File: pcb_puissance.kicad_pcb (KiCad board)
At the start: 2 copper layers, 126.5 x 120.5 mm, 40 parts, among them J1 1755736, J10 Conn_01x02, J11 Conn_01x02, J2 1755736, J3 1755736, J4 1755736, J5 1755736, J6 1755736, J7 1755736, J8 1755736, J9 Conn_01x02, K1 SRD-05VDC-SL-C

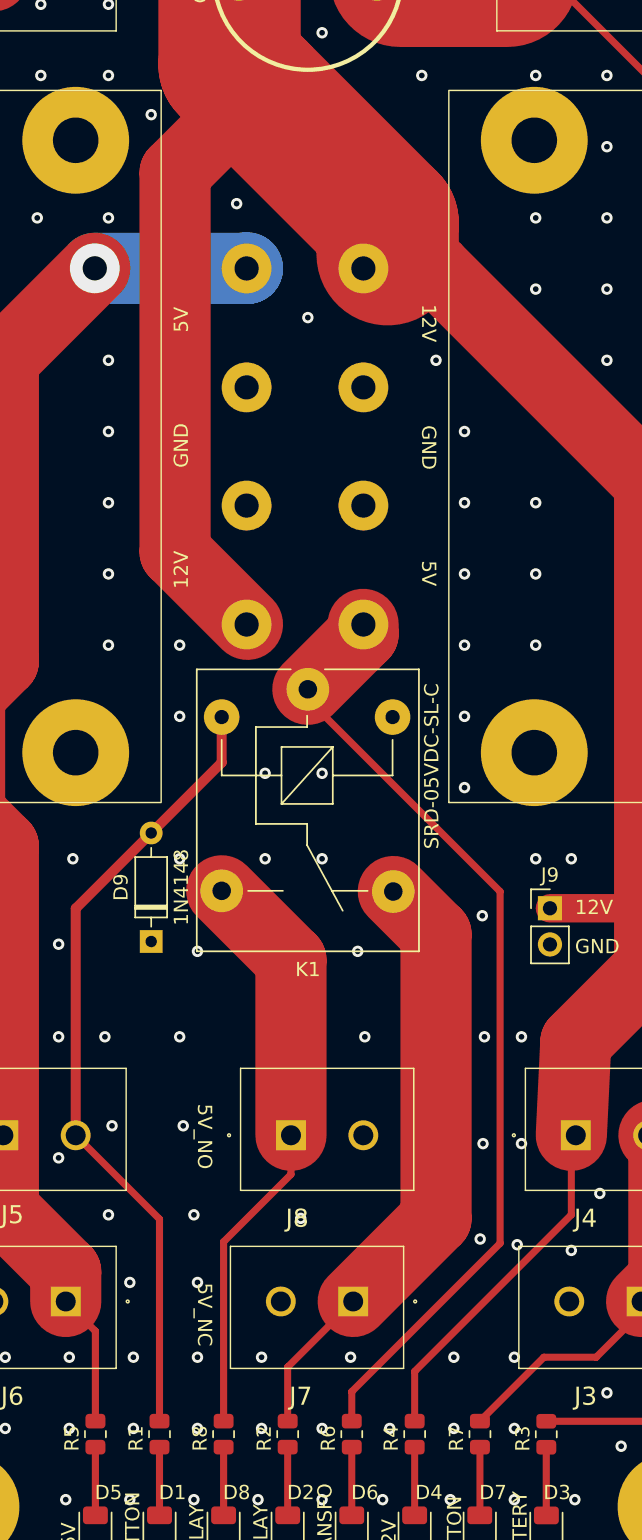
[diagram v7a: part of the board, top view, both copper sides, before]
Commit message: Ajout noms transfos +visibles
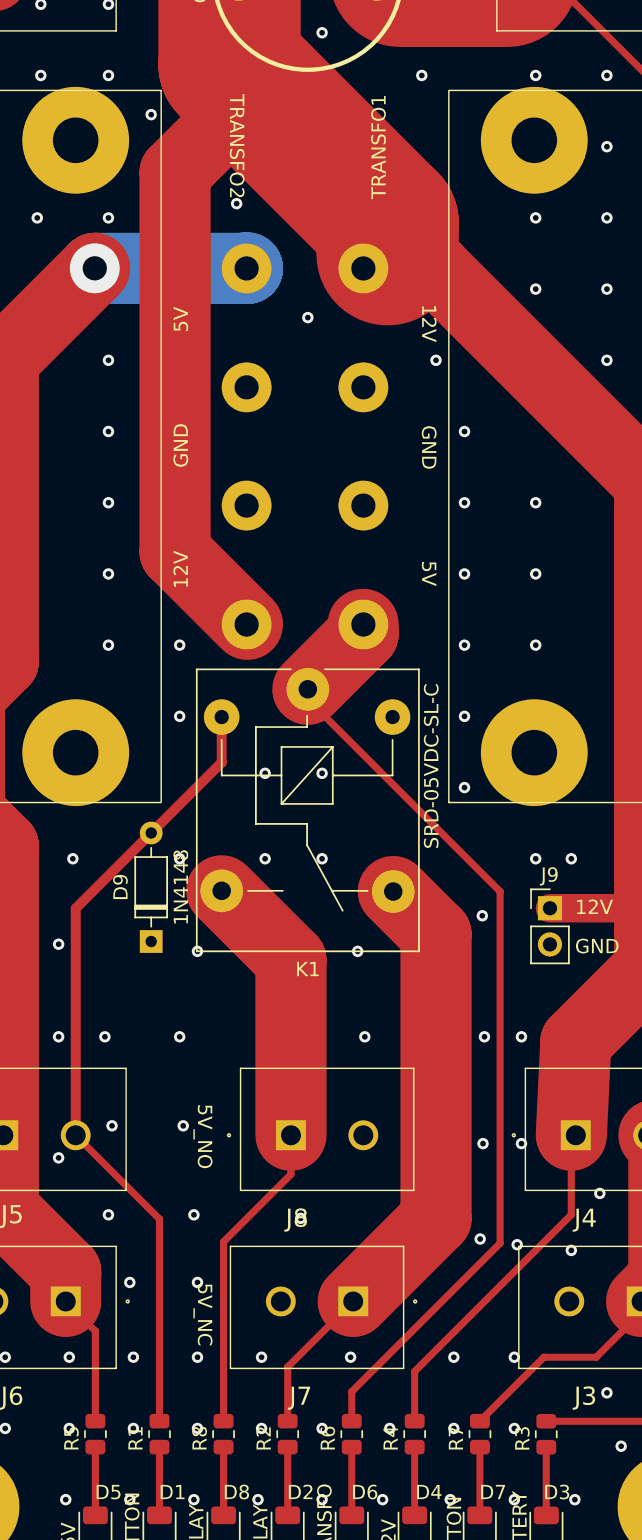
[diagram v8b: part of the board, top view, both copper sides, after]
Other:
- board text added: "TRANSFO1"
- board text added: "TRANSFO2"
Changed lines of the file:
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@@
     (fp_line (start 1 0.625) (end -1 0.625)
       (stroke (width 0.1) (type solid)) (layer "F.Fab"))
-    (pad "1" smd roundrect (at -0.9125 0 90) (size 1.025 1.4) (layers "F.Cu" "F.Paste" "F.Mask") (roundrect_rratio 0.243902)
+    (pad "1" smd roundrect (at -0.9125 0 90) (size 1.025 1.4) (layers "F.Cu" "F.Paste" "F.Mask") (roundrect_rratio 0.243902439)
       (net 9 "Net-(D8-A)") (pintype "passive"))
-    (pad "2" smd roundrect (at 0.9125 0 90) (size 1.025 1.4) (layers "F.Cu" "F.Paste" "F.Mask") (roundrect_rratio 0.243902)
+    (pad "2" smd roundrect (at 0.9125 0 90) (size 1.025 1.4) (layers "F.Cu" "F.Paste" "F.Mask") (roundrect_rratio 0.243902439)
       (net 15 "RELAY_NC") (pintype "passive"))
     (model "${KICAD6_3DMODEL_DIR}/Resistor_SMD.3dshapes/R_0805_2012Metric.wrl"
@@
     (fp_line (start 1 0.625) (end -1 0.625)
       (stroke (width 0.1) (type solid)) (layer "F.Fab"))
-    (pad "1" smd roundrect (at -0.9125 0 90) (size 1.025 1.4) (layers "F.Cu" "F.Paste" "F.Mask") (roundrect_rratio 0.243902)
+    (pad "1" smd roundrect (at -0.9125 0 90) (size 1.025 1.4) (layers "F.Cu" "F.Paste" "F.Mask") (roundrect_rratio 0.243902439)
       (net 5 "Net-(D4-A)") (pintype "passive"))
-    (pad "2" smd roundrect (at 0.9125 0 90) (size 1.025 1.4) (layers "F.Cu" "F.Paste" "F.Mask") (roundrect_rratio 0.243902)
+    (pad "2" smd roundrect (at 0.9125 0 90) (size 1.025 1.4) (layers "F.Cu" "F.Paste" "F.Mask") (roundrect_rratio 0.243902439)
       (net 10 "+12V") (pintype "passive"))
     (model "${KICAD6_3DMODEL_DIR}/Resistor_SMD.3dshapes/R_0805_2012Metric.wrl"
@@
     (fp_line (start 1 0.625) (end -1 0.625)
       (stroke (width 0.1) (type solid)) (layer "F.Fab"))
-    (pad "1" smd roundrect (at -0.9125 0 90) (size 1.025 1.4) (layers "F.Cu" "F.Paste" "F.Mask") (roundrect_rratio 0.243902)
+    (pad "1" smd roundrect (at -0.9125 0 90) (size 1.025 1.4) (layers "F.Cu" "F.Paste" "F.Mask") (roundrect_rratio 0.243902439)
       (net 6 "Net-(D5-A)") (pintype "passive"))
-    (pad "2" smd roundrect (at 0.9125 0 90) (size 1.025 1.4) (layers "F.Cu" "F.Paste" "F.Mask") (roundrect_rratio 0.243902)
+    (pad "2" smd roundrect (at 0.9125 0 90) (size 1.025 1.4) (layers "F.Cu" "F.Paste" "F.Mask") (roundrect_rratio 0.243902439)
       (net 11 "+5V") (pintype "passive"))
     (model "${KICAD6_3DMODEL_DIR}/Resistor_SMD.3dshapes/R_0805_2012Metric.wrl"
@@
     (fp_line (start 1 0.625) (end -1 0.625)
       (stroke (width 0.1) (type solid)) (layer "F.Fab"))
-    (pad "1" smd roundrect (at -0.9125 0 90) (size 1.025 1.4) (layers "F.Cu" "F.Paste" "F.Mask") (roundrect_rratio 0.243902)
+    (pad "1" smd roundrect (at -0.9125 0 90) (size 1.025 1.4) (layers "F.Cu" "F.Paste" "F.Mask") (roundrect_rratio 0.243902439)
       (net 3 "Net-(D2-A)") (pintype "passive"))
-    (pad "2" smd roundrect (at 0.9125 0 90) (size 1.025 1.4) (layers "F.Cu" "F.Paste" "F.Mask") (roundrect_rratio 0.243902)
+    (pad "2" smd roundrect (at 0.9125 0 90) (size 1.025 1.4) (layers "F.Cu" "F.Paste" "F.Mask") (roundrect_rratio 0.243902439)
       (net 14 "RELAY_NO") (pintype "passive"))
     (model "${KICAD6_3DMODEL_DIR}/Resistor_SMD.3dshapes/R_0805_2012Metric.wrl"
@@
     (fp_line (start 1 0.625) (end -1 0.625)
       (stroke (width 0.1) (type solid)) (layer "F.Fab"))
-    (pad "1" smd roundrect (at -0.9125 0 90) (size 1.025 1.4) (layers "F.Cu" "F.Paste" "F.Mask") (roundrect_rratio 0.243902)
+    (pad "1" smd roundrect (at -0.9125 0 90) (size 1.025 1.4) (layers "F.Cu" "F.Paste" "F.Mask") (roundrect_rratio 0.243902439)
       (net 8 "Net-(D7-A)") (pintype "passive"))
-    (pad "2" smd roundrect (at 0.9125 0 90) (size 1.025 1.4) (layers "F.Cu" "F.Paste" "F.Mask") (roundrect_rratio 0.243902)
+    (pad "2" smd roundrect (at 0.9125 0 90) (size 1.025 1.4) (layers "F.Cu" "F.Paste" "F.Mask") (roundrect_rratio 0.243902439)
       (net 17 "BUTTON_NC") (pintype "passive"))
     (model "${KICAD6_3DMODEL_DIR}/Resistor_SMD.3dshapes/R_0805_2012Metric.wrl"
@@
     (fp_line (start 1 0.625) (end -1 0.625)
       (stroke (width 0.1) (type solid)) (layer "F.Fab"))
-    (pad "1" smd roundrect (at -0.9125 0 90) (size 1.025 1.4) (layers "F.Cu" "F.Paste" "F.Mask") (roundrect_rratio 0.243902)
+    (pad "1" smd roundrect (at -0.9125 0 90) (size 1.025 1.4) (layers "F.Cu" "F.Paste" "F.Mask") (roundrect_rratio 0.243902439)
       (net 2 "Net-(D1-A)") (pintype "passive"))
-    (pad "2" smd roundrect (at 0.9125 0 90) (size 1.025 1.4) (layers "F.Cu" "F.Paste" "F.Mask") (roundrect_rratio 0.243902)
+    (pad "2" smd roundrect (at 0.9125 0 90) (size 1.025 1.4) (layers "F.Cu" "F.Paste" "F.Mask") (roundrect_rratio 0.243902439)
       (net 12 "BUTTON_NO") (pintype "passive"))
     (model "${KICAD6_3DMODEL_DIR}/Resistor_SMD.3dshapes/R_0805_2012Metric.wrl"
@@
     (fp_line (start 1 0.625) (end -1 0.625)
       (stroke (width 0.1) (type solid)) (layer "F.Fab"))
-    (pad "1" smd roundrect (at -0.9125 0 90) (size 1.025 1.4) (layers "F.Cu" "F.Paste" "F.Mask") (roundrect_rratio 0.243902)
+    (pad "1" smd roundrect (at -0.9125 0 90) (size 1.025 1.4) (layers "F.Cu" "F.Paste" "F.Mask") (roundrect_rratio 0.243902439)
       (net 4 "Net-(D3-A)") (pintype "passive"))
-    (pad "2" smd roundrect (at 0.9125 0 90) (size 1.025 1.4) (layers "F.Cu" "F.Paste" "F.Mask") (roundrect_rratio 0.243902)
+    (pad "2" smd roundrect (at 0.9125 0 90) (size 1.025 1.4) (layers "F.Cu" "F.Paste" "F.Mask") (roundrect_rratio 0.243902439)
       (net 13 "BATTERY") (pintype "passive"))
     (model "${KICAD6_3DMODEL_DIR}/Resistor_SMD.3dshapes/R_0805_2012Metric.wrl"
@@
     (fp_line (start 1 0.625) (end -1 0.625)
       (stroke (width 0.1) (type solid)) (layer "F.Fab"))
-    (pad "1" smd roundrect (at -0.9125 0 90) (size 1.025 1.4) (layers "F.Cu" "F.Paste" "F.Mask") (roundrect_rratio 0.243902)
+    (pad "1" smd roundrect (at -0.9125 0 90) (size 1.025 1.4) (layers "F.Cu" "F.Paste" "F.Mask") (roundrect_rratio 0.243902439)
       (net 7 "Net-(D6-A)") (pintype "passive"))
-    (pad "2" smd roundrect (at 0.9125 0 90) (size 1.025 1.4) (layers "F.Cu" "F.Paste" "F.Mask") (roundrect_rratio 0.243902)
+    (pad "2" smd roundrect (at 0.9125 0 90) (size 1.025 1.4) (layers "F.Cu" "F.Paste" "F.Mask") (roundrect_rratio 0.243902439)
       (net 16 "TRANSFO1") (pintype "passive"))
     (model "${KICAD6_3DMODEL_DIR}/Resistor_SMD.3dshapes/R_0805_2012Metric.wrl"
@@
     (effects (font (size 1 1) (thickness 0.15)) (justify left bottom))
   )
+  (gr_text "TRANSFO2" (at 79 45 270) (layer "F.SilkS")
+    (effects (font (size 1 1) (thickness 0.15)))
+  )
   (gr_text "GND\n" (at 56.5 100) (layer "F.SilkS")
     (effects (font (size 1 1) (thickness 0.15)) (justify left bottom))
@@
     (effects (font (size 1 1) (thickness 0.15)) (justify left bottom))
   )
+  (gr_text "TRANSFO1" (at 89 45 90) (layer "F.SilkS")
+    (effects (font (size 1 1) (thickness 0.15)))
+  )
   (gr_text "Carte de puissance V1\nMODELEC ISEN 2024" (at 109.5 102.5) (layer "F.SilkS")
